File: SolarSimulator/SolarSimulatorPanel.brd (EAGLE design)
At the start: 155.7 x 75.2 mm, 79 parts, among them U1 Red Driver, U2 Green Driver, U3 Blue Driver, X1 MKDSN1,5/2-5,08

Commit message: tweaks on solar simulator board
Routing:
- net N$2: track 33.5 -> 28.8 mm
- net N$93: track 141.5 -> 139.5 mm
- net N$77: track 14.1 -> 15.4 mm
- net PWM_R: track 128.8 -> 127.6 mm
- net N$19: track 12.8 -> 11.7 mm
- net N$53: track 2.94 -> 3.73 mm
- net VPP: track 144.2 -> 143.8 mm, vias 13 -> 12

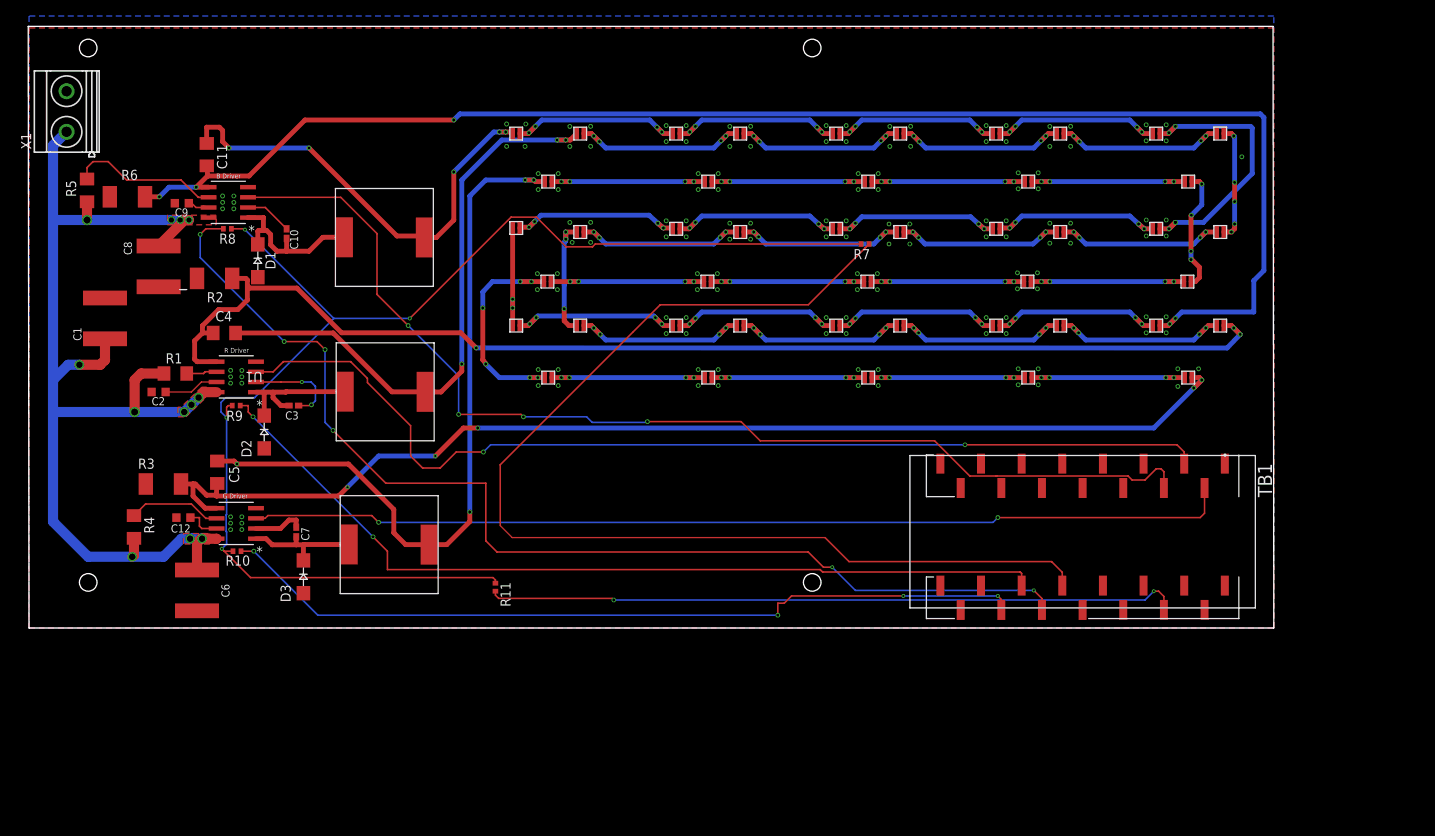
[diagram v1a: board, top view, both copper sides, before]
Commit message: Outline, ground plane, and DXF cleanup.
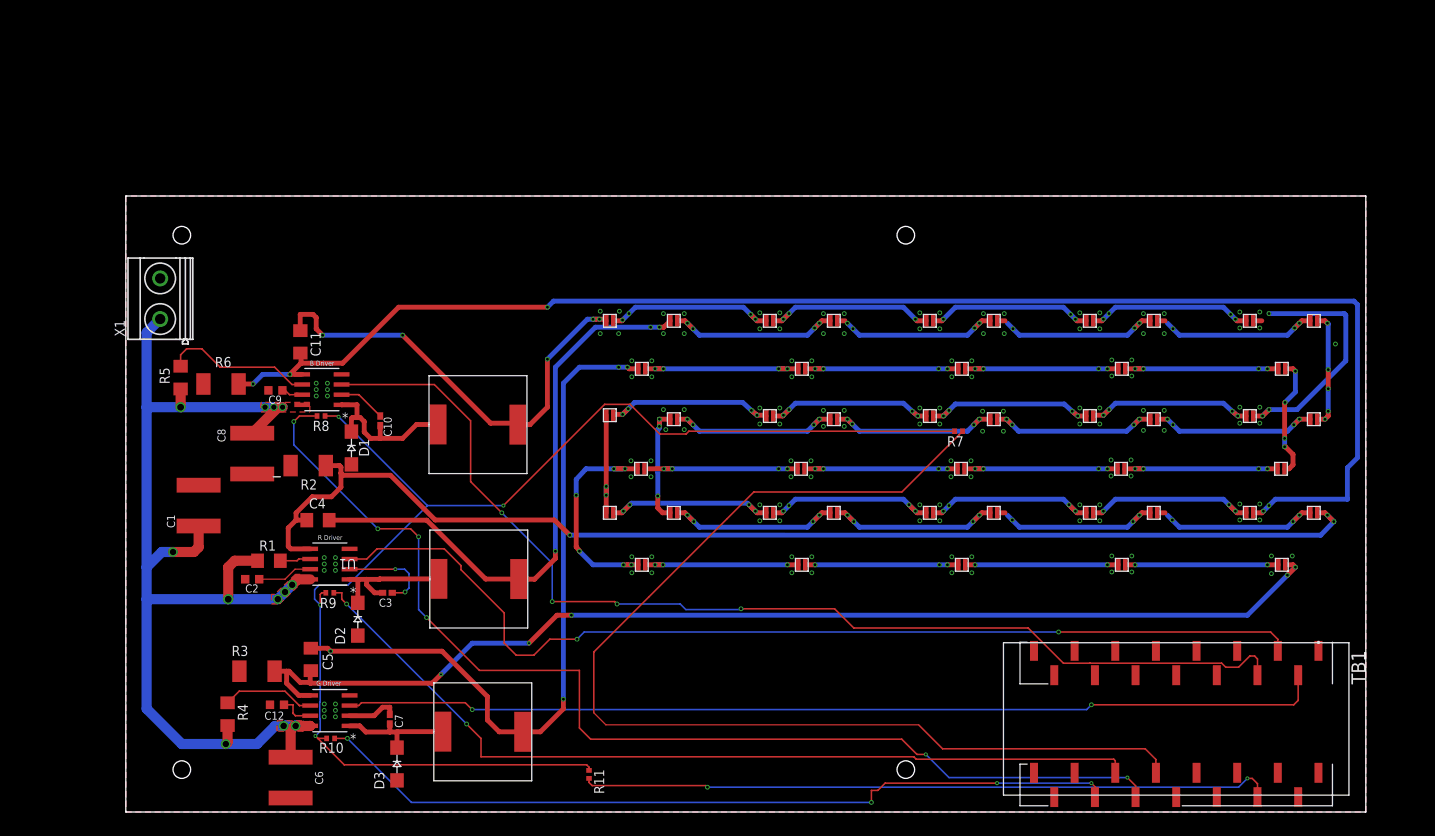
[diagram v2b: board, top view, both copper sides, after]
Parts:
- moved BLUE6 26.2 mm to (141.3, 50.3)
- moved BLUE7 26.2 mm to (121.3, 50.3)
- moved BLUE8 26.2 mm to (101.3, 50.3)
- moved BLUE9 26.2 mm to (81.3, 50.3)
- moved C8 26.2 mm to (15.8, 44.8)
- moved R2 26.2 mm to (22.8, 43.3)
- moved R6 26.2 mm to (11.9, 53.5)
- moved RED5 26.2 mm to (149.3, 49.9)
- moved RED6 26.2 mm to (129.3, 49.9)
- moved TB1 26.2 mm to (131.3, 11.0)
- moved U3 26.2 mm to (24.5, 52.8)
- moved L3 26.2 mm to (38.5, 3.90)
- moved R1 26.2 mm to (17.9, 31.4)
- moved R10 26.2 mm to (25.6, 9.20)
- moved R4 26.2 mm to (12.7, 12.2)
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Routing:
- net N$56: track 35.2 -> 32.0 mm, vias 4 -> 3
- net N$15: track 22.4 -> 21.0 mm
- net N$16: track 22.4 -> 21.0 mm
- net N$17: track 22.4 -> 21.0 mm
- net N$12: track 22.6 -> 21.3 mm
- net N$13: track 22.6 -> 21.3 mm
- net N$39: track 21.2 -> 20.1 mm
- net N$144: track 1.05 -> 0.00 mm
- net N$152: track 1.05 -> 0.00 mm
- net N$150: track 1.05 -> 0.00 mm
- net N$148: track 1.05 -> 0.00 mm
- net N$147: track 1.05 -> 0.00 mm
- net N$145: track 1.05 -> 0.00 mm
- net N$142: track 1.05 -> 0.00 mm
- net N$140: track 1.05 -> 0.00 mm
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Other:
- board size 155.7 x 75.2 mm -> 155 x 77 mm

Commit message: layout clean up for better ground path and some OCD.
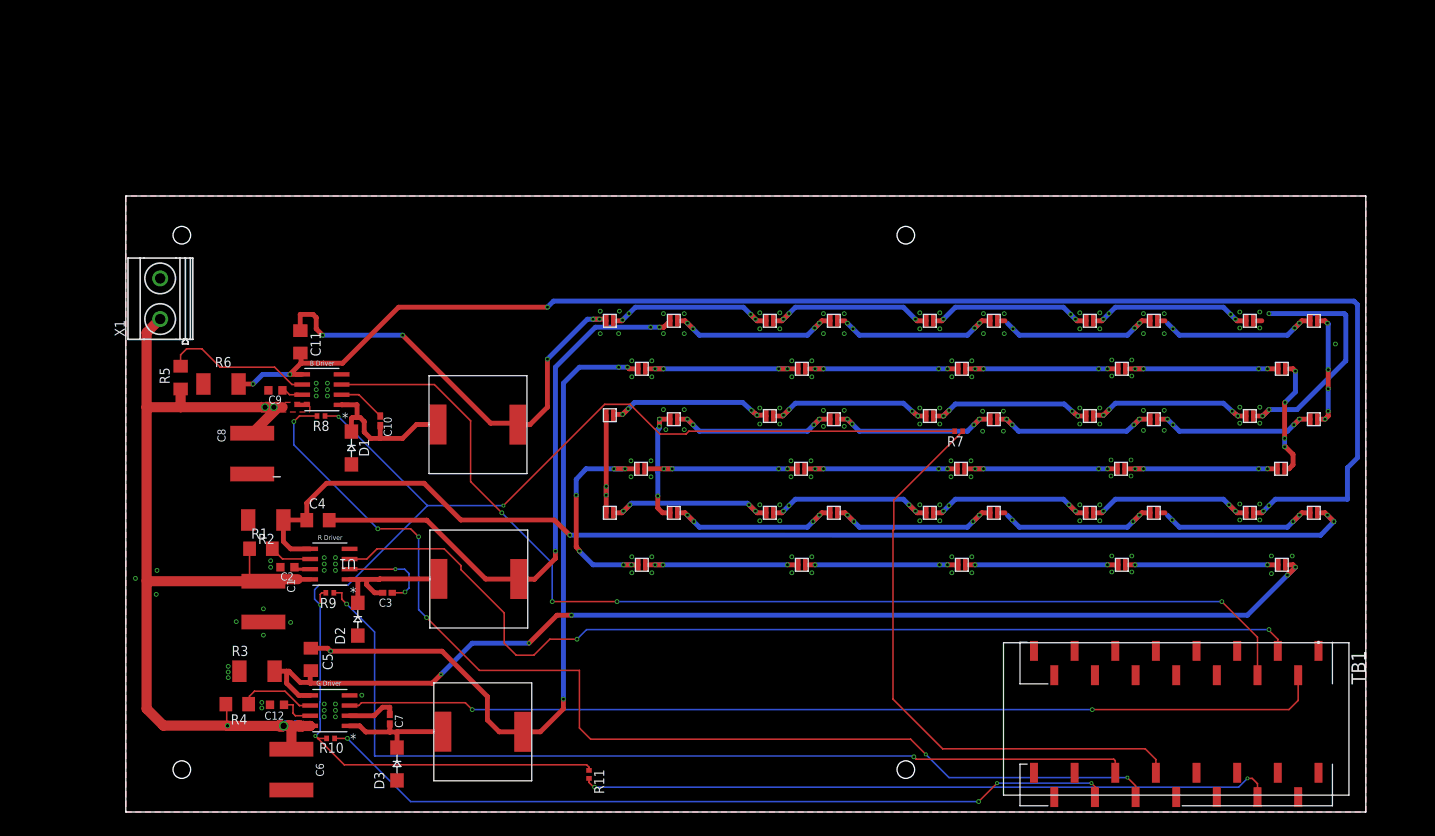
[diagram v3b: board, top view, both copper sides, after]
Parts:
- moved C1 14.5 mm to (17.2, 26.3), turned to 270 degrees
- moved R2 8.62 mm to (17.5, 36.5)
- moved C2 4.65 mm to (20.2, 30.6)
- moved R1 1.80 mm to (16.9, 32.9)
- moved R4 1.74 mm to (13.9, 13.5), turned to 180 degrees
- moved C6 1.00 mm to (20.7, 5.30)
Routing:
- net N$93: track 139.5 -> 74.7 mm
- net VPP: track 143.8 -> 125.6 mm, vias 12 -> 5
- net N$58: track 109.7 -> 117.4 mm
- net N$4: track 6.89 -> 2.07 mm
- net N$79: track 151.9 -> 147.9 mm
- net N$19: track 11.7 -> 9.63 mm
- net N$6: track 3.83 -> 5.27 mm
- net N$51: track 101.7 -> 100.8 mm

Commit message: Beeeg cleanup. Converted passives to RCL custom, cleaned up switcher layout, started the Big Stitch, and cleaned up where possible. Left to do: LED footprint cleanup, and routing to dump their heat to a ground pad below them.
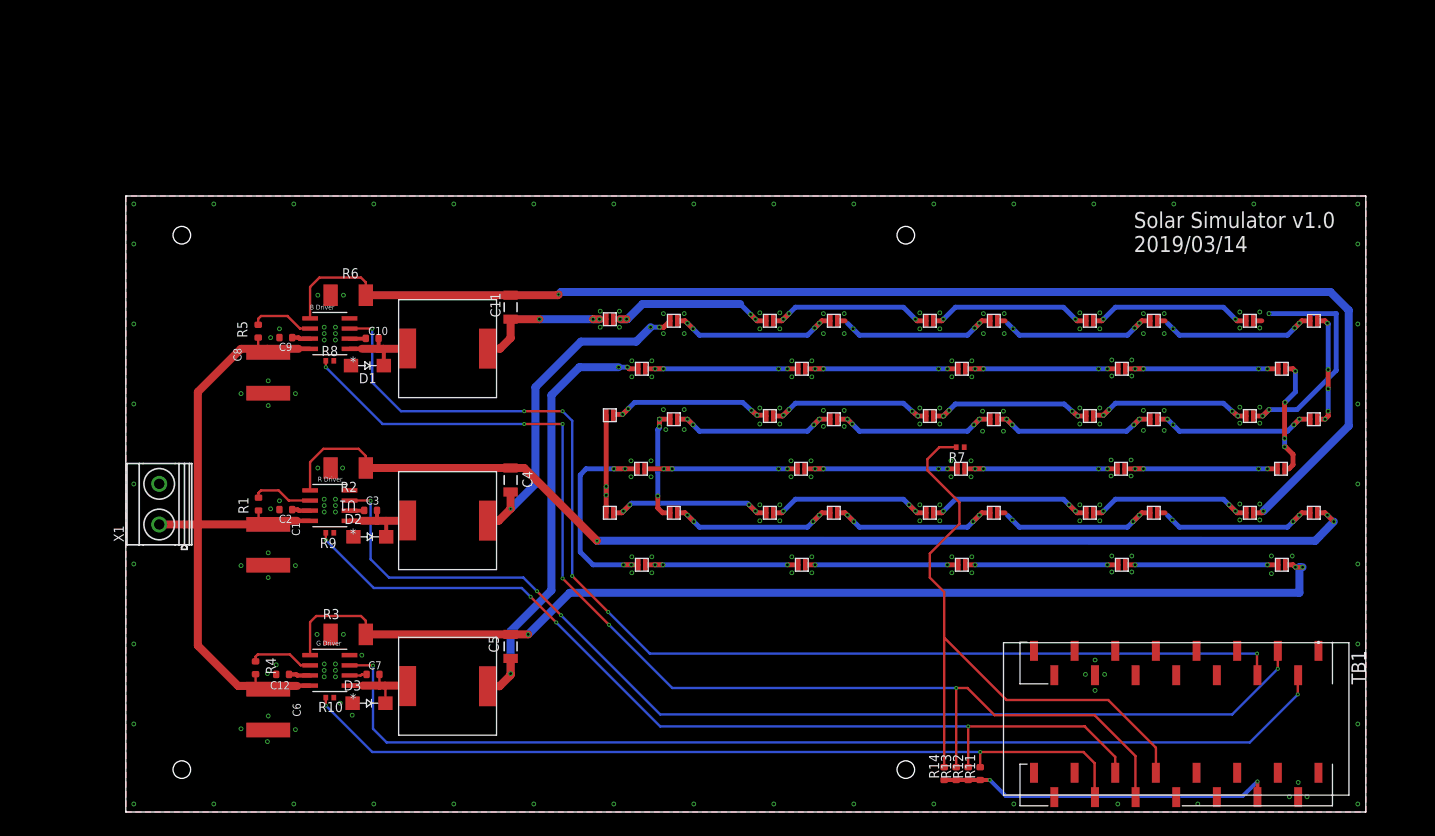
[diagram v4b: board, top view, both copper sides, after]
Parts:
- added R12, R13, R14: 10k, oresat-rcl:.0603-B-NOSILK
- C10, C3, C7: value (none) -> 10n 25V; device rcl:C0402K -> oresat-rcl:.0603-B-NOSILK
- C11, C4, C5: device rcl:C1206 -> oresat-rcl:1206-B
- C12, C2, C9: value (none) -> 100n 25V; device rcl:C0603K -> oresat-rcl:.0603-B-NOSILK
- R1, R4, R5: device rcl:R1206 -> oresat-rcl:.0603-B-NOSILK
- R11: device solarsim:R0402 -> oresat-rcl:.0603-B-NOSILK
- moved R11 48.9 mm to (106.8, 4.80), turned to 90 degrees
- moved C11 26.6 mm to (48.1, 63.1), turned to 90 degrees
- moved X1 25.7 mm to (4.20, 38.5)
- moved C5 25.0 mm to (48.1, 20.7), turned to 90 degrees
- moved C4 24.6 mm to (48.1, 41.5), turned to 90 degrees
- moved R6 19.4 mm to (27.8, 64.6)
- moved R3 12.3 mm to (27.8, 22.2)
- moved R2 12.2 mm to (27.8, 43.0)
- moved R5 11.3 mm to (16.6, 60.1)
- moved C3 10.5 mm to (30.6, 37.7), turned to 0 degrees
- moved D1 10.5 mm to (30.2, 55.8), turned to 0 degrees
- moved D2 10.4 mm to (30.5, 34.4), turned to 0 degrees
- moved C10 10.3 mm to (30.8, 59.2), turned to 0 degrees
- moved C8 10.3 mm to (17.8, 54.9)
- moved L1 10.2 mm to (34.1, 51.8)
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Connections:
- net N$28 renamed GREEN-RTN
- net N$3 renamed RED-OUT
- net N$54 renamed BLUE-RTN
- net N$55 renamed BLUE-OUT
- net N$79 renamed RED-RTN
- net N$80 renamed GRN-OUT
- removed net N$47: R11.2, TB1.57
- removed net N$51: R10.1, TB1.49
- removed net N$58: R9.1, TB1.50
- removed net N$59: R8.1, TB1.51
- removed net N$93: R7.1, TB1.52
- new net +5V: R11.1, R12.1, R13.1, R14.1, TB1.57
- new net N$60: R14.2, R7.2, TB1.52
- new net N$61: R13.2, R8.2, TB1.51
- new net N$62: R12.2, R9.2, TB1.50
- net GND: now also R10.1, R7.1, R8.1, R9.1
- net N$91: now also R11.2, TB1.49; no longer R11.1, R7.2, R8.2, R9.2
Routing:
- net N$61: track 0.00 -> 148.5 mm, vias 0 -> 6
- net N$59: track 139.9 -> 0.00 mm, vias 6 -> 0
- net N$62: track 0.00 -> 117.9 mm, vias 0 -> 4
- net N$58: track 117.4 -> 0.00 mm, vias 2 -> 0
- net N$51: track 100.8 -> 0.00 mm, vias 4 -> 0
- net N$47: track 86.7 -> 0.00 mm, vias 2 -> 0
- net N$60: track 0.00 -> 82.0 mm
- net N$93: track 74.7 -> 0.00 mm
- net N$91: track 167.0 -> 106.2 mm, vias 4 -> 2
- net +5V: track 0.00 -> 42.7 mm, vias 0 -> 2
- net BLUE-OUT: track 56.7 -> 18.5 mm, vias 5 -> 3
- net VPP: track 125.6 -> 88.9 mm, vias 5 -> 0
- net GRN-OUT: track 89.8 -> 54.9 mm, vias 4 -> 3
- net RED-OUT: track 73.1 -> 42.4 mm
- net BLUE-RTN: track 184.5 -> 168.1 mm, vias 4 -> 2
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- removed copper zone on layer 1, net VPP
- removed copper zone on layer 16, net VPP
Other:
- board text added: "2019/03/14"
- board text added: "Solar Simulator v1.0"
